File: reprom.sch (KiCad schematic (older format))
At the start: 14 parts, among them P1 KERNAL_SOCKET, P2 KERNAL_AND_BASIC_SOCKET, P3 LEFT_SOCKET, P4 RIGHT_SOCKET, P5 KERNAL, P6 CHARSET, P7 BASIC, U1 27512, U2 GAL16V8

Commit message: Hardware: Removed crappy autorouting, improved part placement
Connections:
- net BS: now also JP1.3; no longer JP1.1
- net CS: now also JP1.1; no longer JP1.3
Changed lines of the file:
@@
 Text Label 4750 1200 3    60   ~ 0
 BCS
+Text Label 5000 1100 0    60   ~ 0
+BS
 Text Label 4500 1100 2    60   ~ 0
-BS
-Text Label 5000 1100 0    60   ~ 0
 CS
 $Comp

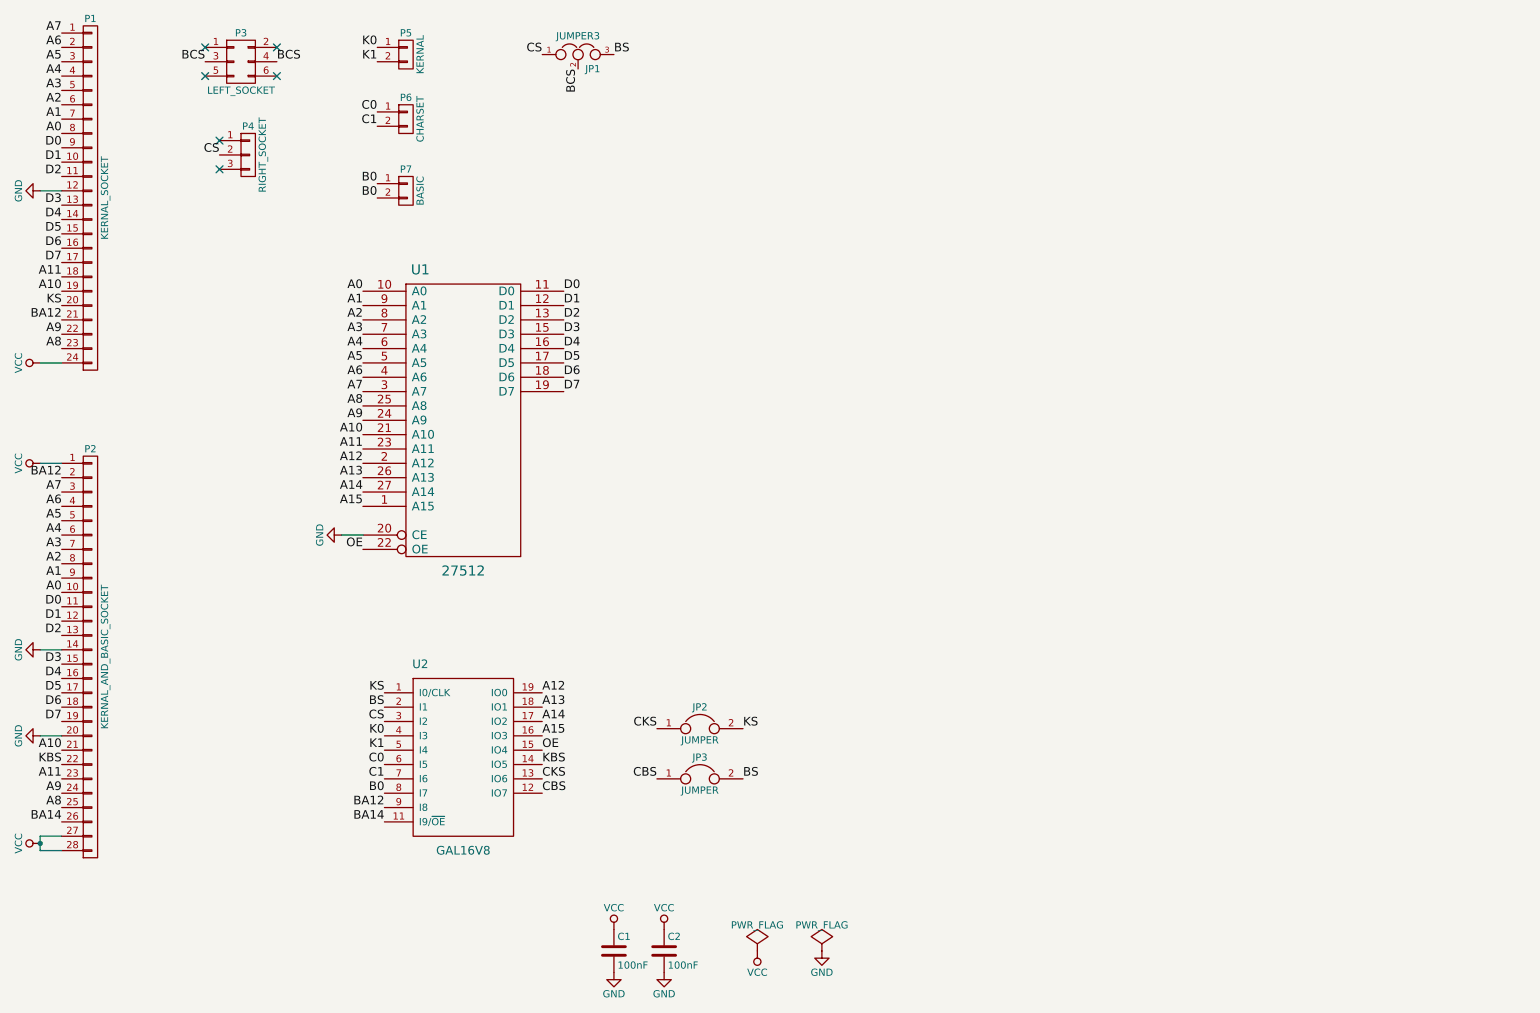
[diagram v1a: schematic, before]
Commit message: Hardware: Improved routing, designed silkscreen, improved schematics
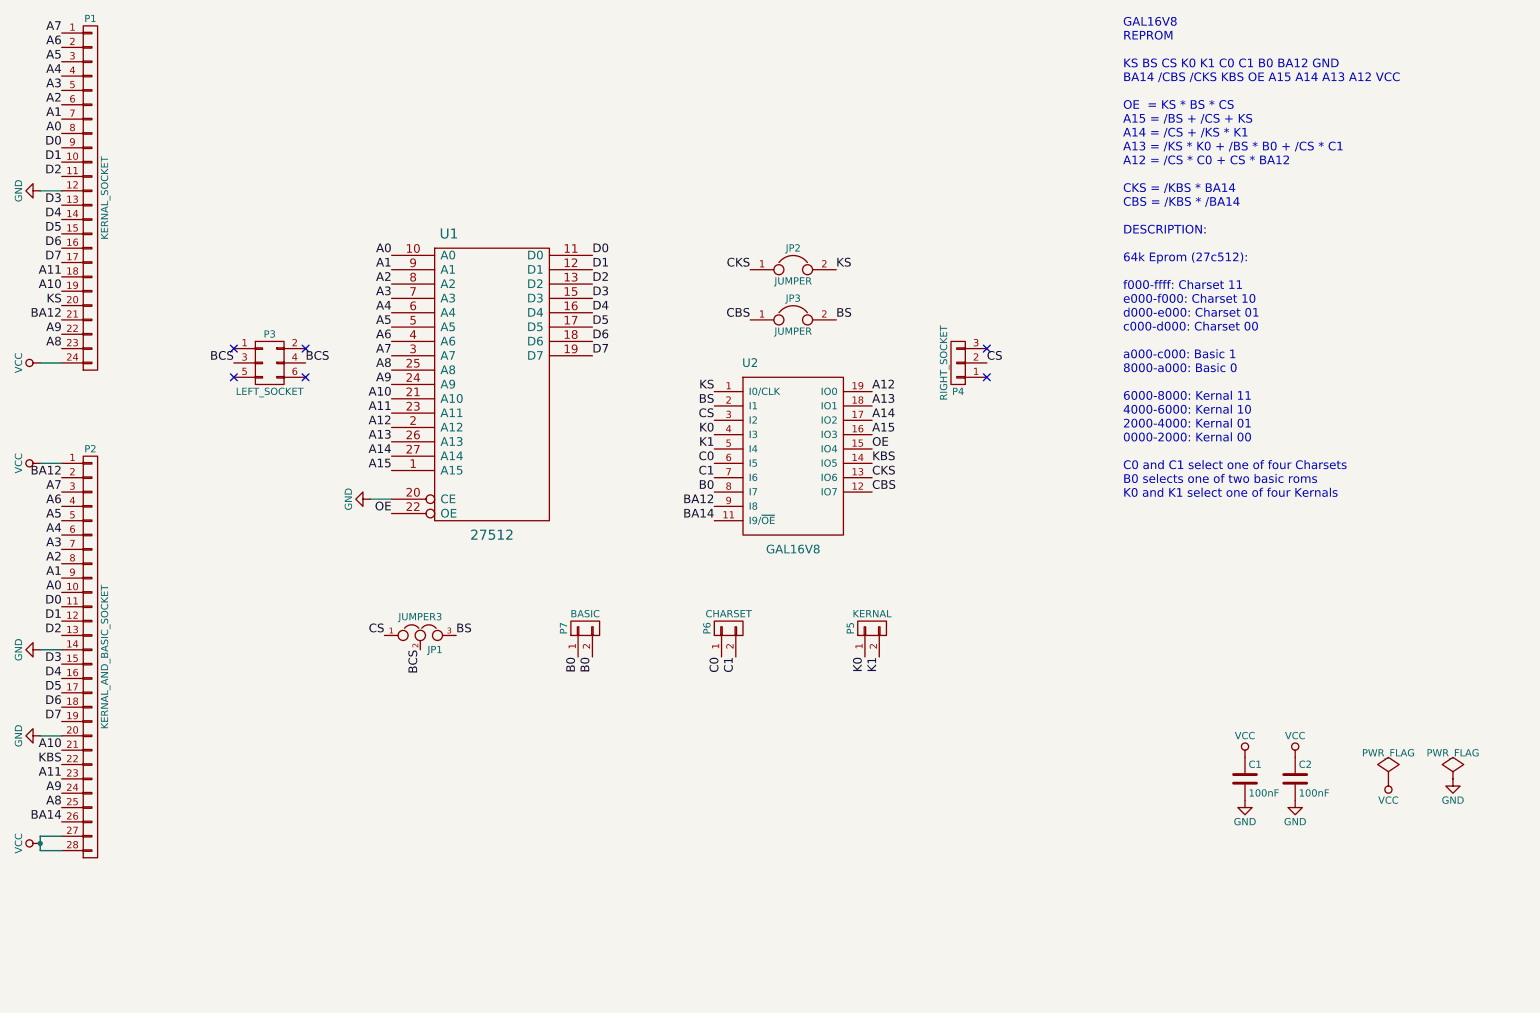
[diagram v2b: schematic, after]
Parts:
- P1: footprint Housings_DIP:DIP-24_W15.24mm -> custom:DIP-24_W15.24mm
- P2, U1: footprint Housings_DIP:DIP-28_W15.24mm -> custom:DIP-28_W15.24mm
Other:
- note added: "GAL16V8\nREPROM\n\nKS BS CS K0 K1 C0 C1 B0 BA12 GND\nBA14 /CBS /CKS KBS OE A15 A14 A13 A12 VCC\n\nOE = KS * BS * CS\nA15 = /BS + /CS + KS\nA14 = /CS + /KS * K1\nA13 = /KS * K0 + /BS * B0 + /CS * C1\nA12 = /CS * C0 + CS * BA12\n\nCKS = /KBS * BA14\nCBS = /KBS * /BA14\n\nDESCRIPTION:\n\n64k Eprom (27c512):\n\nf000-ffff: Charset 11\ne000-f000: Charset 10\nd000-e000: Charset 01\nc000-d000: Charset 00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"
- moved on the sheet: C1, C2, JP1, JP2, JP3, P3, P4, P5, P6, P7, U1, U2

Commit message: Hardware: Added additional pin headers for wider rom layouts (KU/326298)
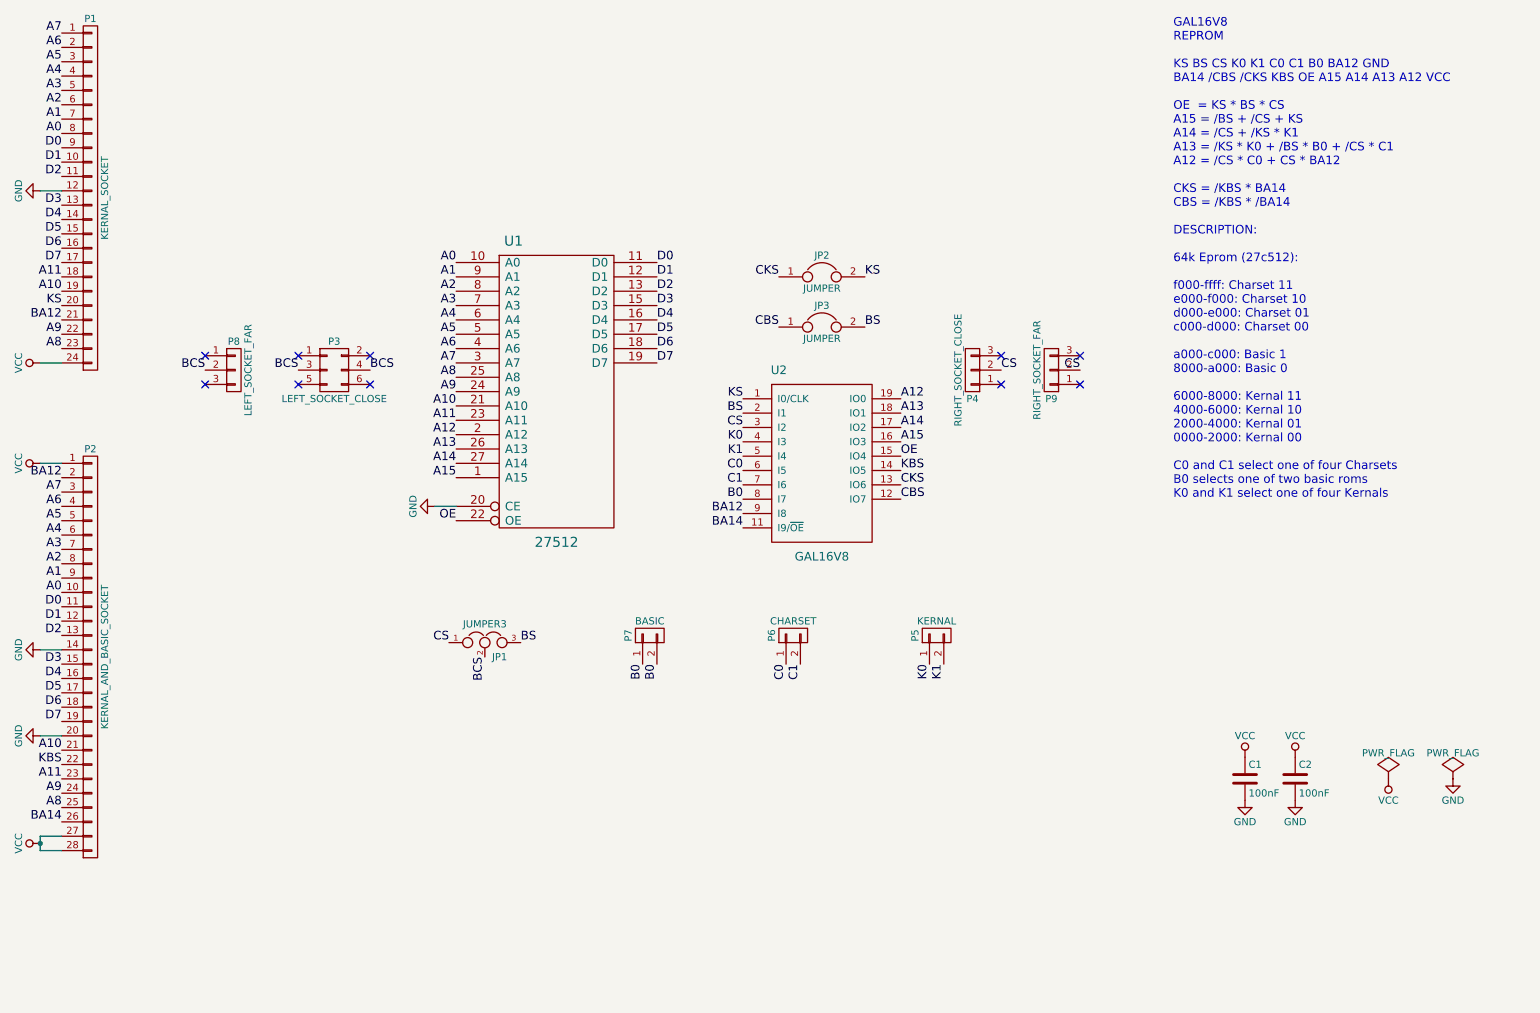
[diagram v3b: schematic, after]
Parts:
- added P8: LEFT_SOCKET_FAR, custom:Pin_Header_Straight_1x03, symbol CONN_01X03
- added P9: RIGHT_SOCKET_FAR, custom:Pin_Header_Straight_1x03, symbol CONN_01X03
- P3: value LEFT_SOCKET -> LEFT_SOCKET_CLOSE; footprint Pin_Headers:Pin_Header_Straight_2x03 -> custom:Pin_Header_Straight_2x03
- P4: value RIGHT_SOCKET -> RIGHT_SOCKET_CLOSE; footprint Pin_Headers:Pin_Header_Straight_1x03 -> custom:Pin_Header_Straight_1x03
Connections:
- net BCS: now also P8.2 (P2)
- net CS: now also P9.2 (P2)
- no-connect marks 6 -> 10
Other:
- moved on the sheet: JP1, JP2, JP3, P3, P4, P5, P6, P7, U1, U2

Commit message: Revert "Hardware: Added additional pin headers for wider rom layouts (KU/326298)"
This reverts commit 2e8d7ef8814329ef0b47112793623fe7f19c62f6.
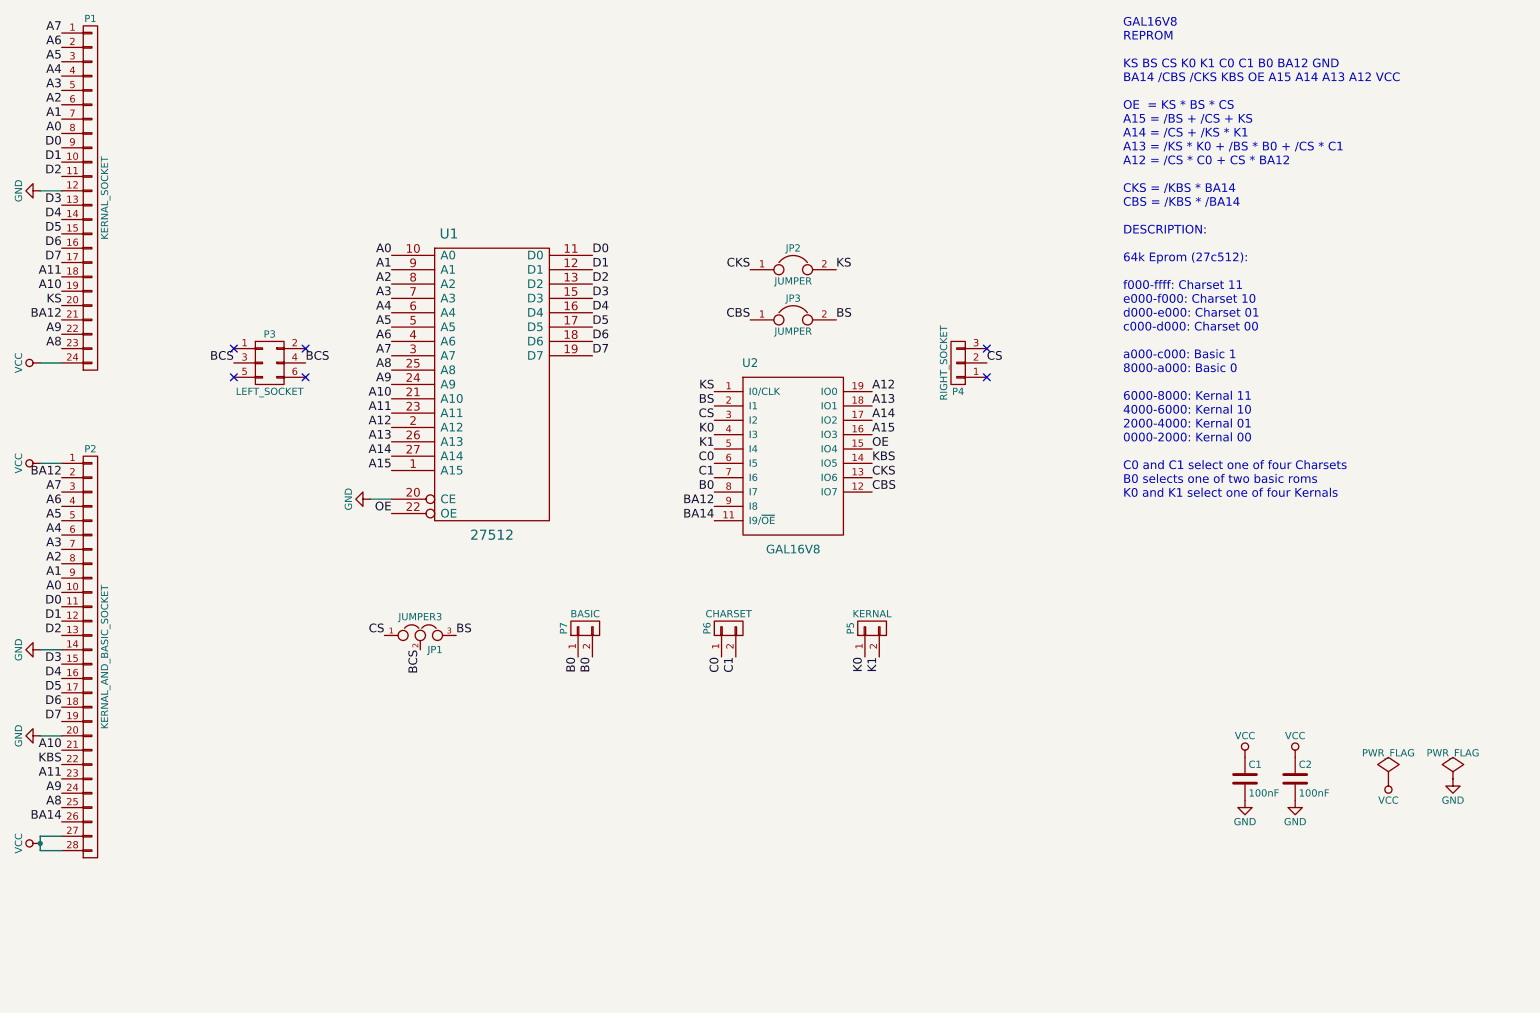
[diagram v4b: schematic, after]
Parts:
- removed P8: LEFT_SOCKET_FAR, custom:Pin_Header_Straight_1x03, symbol CONN_01X03
- removed P9: RIGHT_SOCKET_FAR, custom:Pin_Header_Straight_1x03, symbol CONN_01X03
- P3: value LEFT_SOCKET_CLOSE -> LEFT_SOCKET; footprint custom:Pin_Header_Straight_2x03 -> Pin_Headers:Pin_Header_Straight_2x03
- P4: value RIGHT_SOCKET_CLOSE -> RIGHT_SOCKET; footprint custom:Pin_Header_Straight_1x03 -> Pin_Headers:Pin_Header_Straight_1x03
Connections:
- no-connect marks 10 -> 6
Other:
- moved on the sheet: JP1, JP2, JP3, P3, P4, P5, P6, P7, U1, U2

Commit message: Hardware: Added support for all board types
This adds the pin headers required to use the adapter
on ancient boards (396298 and KU14194HB) and on the
SX64 CPU board (251102).
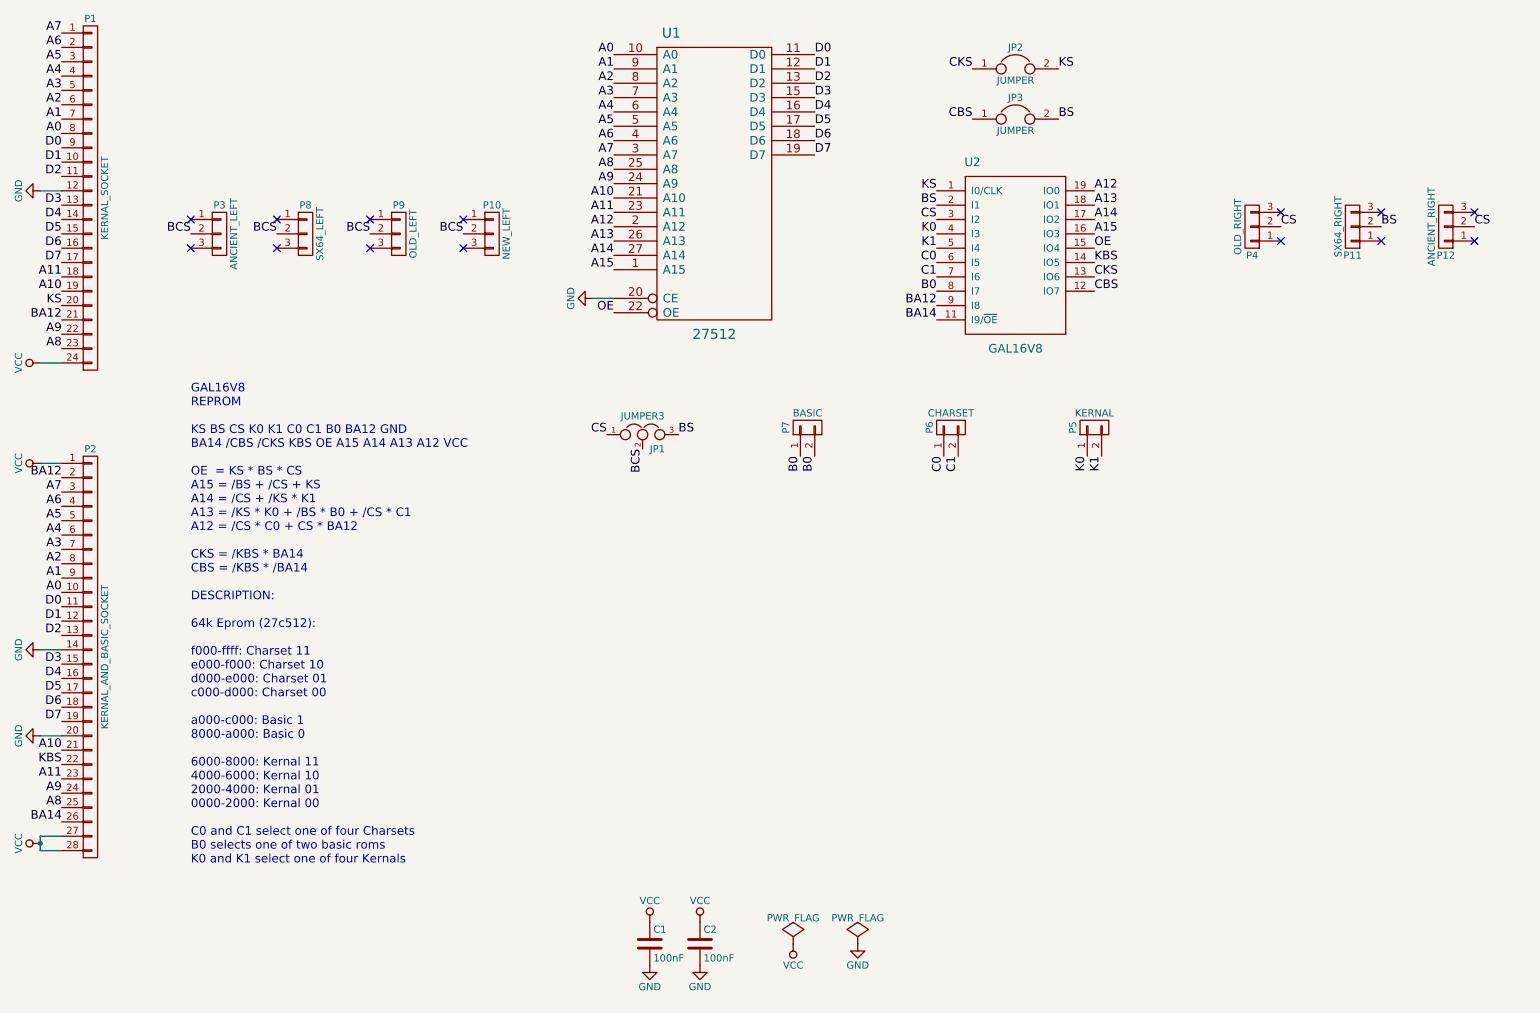
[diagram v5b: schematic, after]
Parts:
- removed P3: LEFT_SOCKET, Pin_Headers:Pin_Header_Straight_2x03, symbol CONN_02X03
- added P10: NEW_LEFT, custom:Pin_Header_Straight_1x03, symbol CONN_01X03
- added P11: SX64_RIGHT, custom:Pin_Header_Straight_1x03, symbol CONN_01X03
- added P12: ANCIENT_RIGHT, custom:Pin_Header_Straight_1x03, symbol CONN_01X03
- added P3: ANCIENT_LEFT, custom:Pin_Header_Straight_1x03, symbol CONN_01X03
- added P8: SX64_LEFT, custom:Pin_Header_Straight_1x03, symbol CONN_01X03
- added P9: OLD_LEFT, custom:Pin_Header_Straight_1x03, symbol CONN_01X03
- P4: value RIGHT_SOCKET -> OLD_RIGHT; footprint Pin_Headers:Pin_Header_Straight_1x03 -> custom:Pin_Header_Straight_1x03
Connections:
- net BCS: now also P10.2 (P2), P3.2 (P2), P8.2 (P2), P9.2 (P2)
- net BS: now also P11.2 (P2)
- net CS: now also P12.2 (P2)
- no-connect marks 6 -> 14
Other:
- moved on the sheet: C1, C2, JP1, JP2, JP3, P4, P5, P6, P7, U1, U2

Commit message: Hardware: Added GND connector, improved layout, silkscreen and 3d view
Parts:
- added P13: GND, custom:Pin_Header_Straight_1x01, symbol CONN_01X01
- U1: symbol 27512 -> 27512-RESCUE-reprom
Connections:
- net GND: now also P13.1 (P1)
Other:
- moved on the sheet: P6, P7
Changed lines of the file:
@@
 EESchema Schematic File Version 2
+LIBS:reprom-rescue
 LIBS:power
 LIBS:device
@@
 $EndDescr
 $Comp
-L 27512 U1
+L 27512-RESCUE-reprom U1
 U 1 1 569CC8CC
 P 5700 2000
@@
 L CONN_01X02 P6
 U 1 1 569CE3B5
-P 7350 3700
-F 0 "P6" H 7350 3850 50  0000 C CNN
-F 1 "CHARSET" V 7450 3700 50  0000 C CNN
-F 2 "Pin_Headers:Pin_Header_Straight_1x02" H 7350 3700 60  0001 C CNN
-F 3 "" H 7350 3700 60  0000 C CNN
-	1    7350 3700
+P 7650 3700
+F 0 "P6" H 7650 3850 50  0000 C CNN
+F 1 "CHARSET" V 7750 3700 50  0000 C CNN
+F 2 "Pin_Headers:Pin_Header_Straight_1x02" H 7650 3700 60  0001 C CNN
+F 3 "" H 7650 3700 60  0000 C CNN
+	1    7650 3700
 	0    -1   -1   0
 $EndComp
-Text Label 7300 3900 3    60   ~ 0
+Text Label 7600 3900 3    60   ~ 0
 C0
-Text Label 7400 3900 3    60   ~ 0
+Text Label 7700 3900 3    60   ~ 0
 C1
 $Comp
 L CONN_01X02 P7
 U 1 1 569CE4F5
-P 6350 3700
-F 0 "P7" H 6350 3850 50  0000 C CNN
-F 1 "BASIC" V 6450 3700 50  0000 C CNN
-F 2 "Pin_Headers:Pin_Header_Straight_1x02" H 6350 3700 60  0001 C CNN
-F 3 "" H 6350 3700 60  0000 C CNN
-	1    6350 3700
+P 6950 3700
+F 0 "P7" H 6950 3850 50  0000 C CNN
+F 1 "BASIC" V 7050 3700 50  0000 C CNN
+F 2 "Pin_Headers:Pin_Header_Straight_1x02" H 6950 3700 60  0001 C CNN
+F 3 "" H 6950 3700 60  0000 C CNN
+	1    6950 3700
 	0    -1   -1   0
 $EndComp
-Text Label 6300 3900 3    60   ~ 0
+Text Label 6900 3900 3    60   ~ 0
 B0
-Text Label 6400 3900 3    60   ~ 0
+Text Label 7000 3900 3    60   ~ 0
 B0
 Text Label 7250 2050 2    60   ~ 0
@@
 Text Label 10350 2300 0    60   ~ 0
 BS
+$Comp
+L CONN_01X01 P13
+U 1 1 574B08B5
+P 6150 3750
+F 0 "P13" H 6150 3850 50  0000 C CNN
+F 1 "GND" V 6250 3750 50  0000 C CNN
+F 2 "custom:Pin_Header_Straight_1x01" H 6150 3750 50  0001 C CNN
+F 3 "" H 6150 3750 50  0000 C CNN
+	1    6150 3750
+	0    -1   -1   0
+$EndComp
+$Comp
+L GND #PWR016
+U 1 1 574B0AE9
+P 6150 3950
+F 0 "#PWR016" H 6150 3700 50  0001 C CNN
+F 1 "GND" H 6150 3800 50  0000 C CNN
+F 2 "" H 6150 3950 50  0000 C CNN
+F 3 "" H 6150 3950 50  0000 C CNN
+	1    6150 3950
+	1    0    0    -1
+$EndComp
 $EndSCHEMATC
